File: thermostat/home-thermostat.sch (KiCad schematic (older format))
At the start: 12 parts, among them J1 Thermosthat, U3 LM2574M-5, U4 LD1117S33TR_SOT223, U5 AT24C512

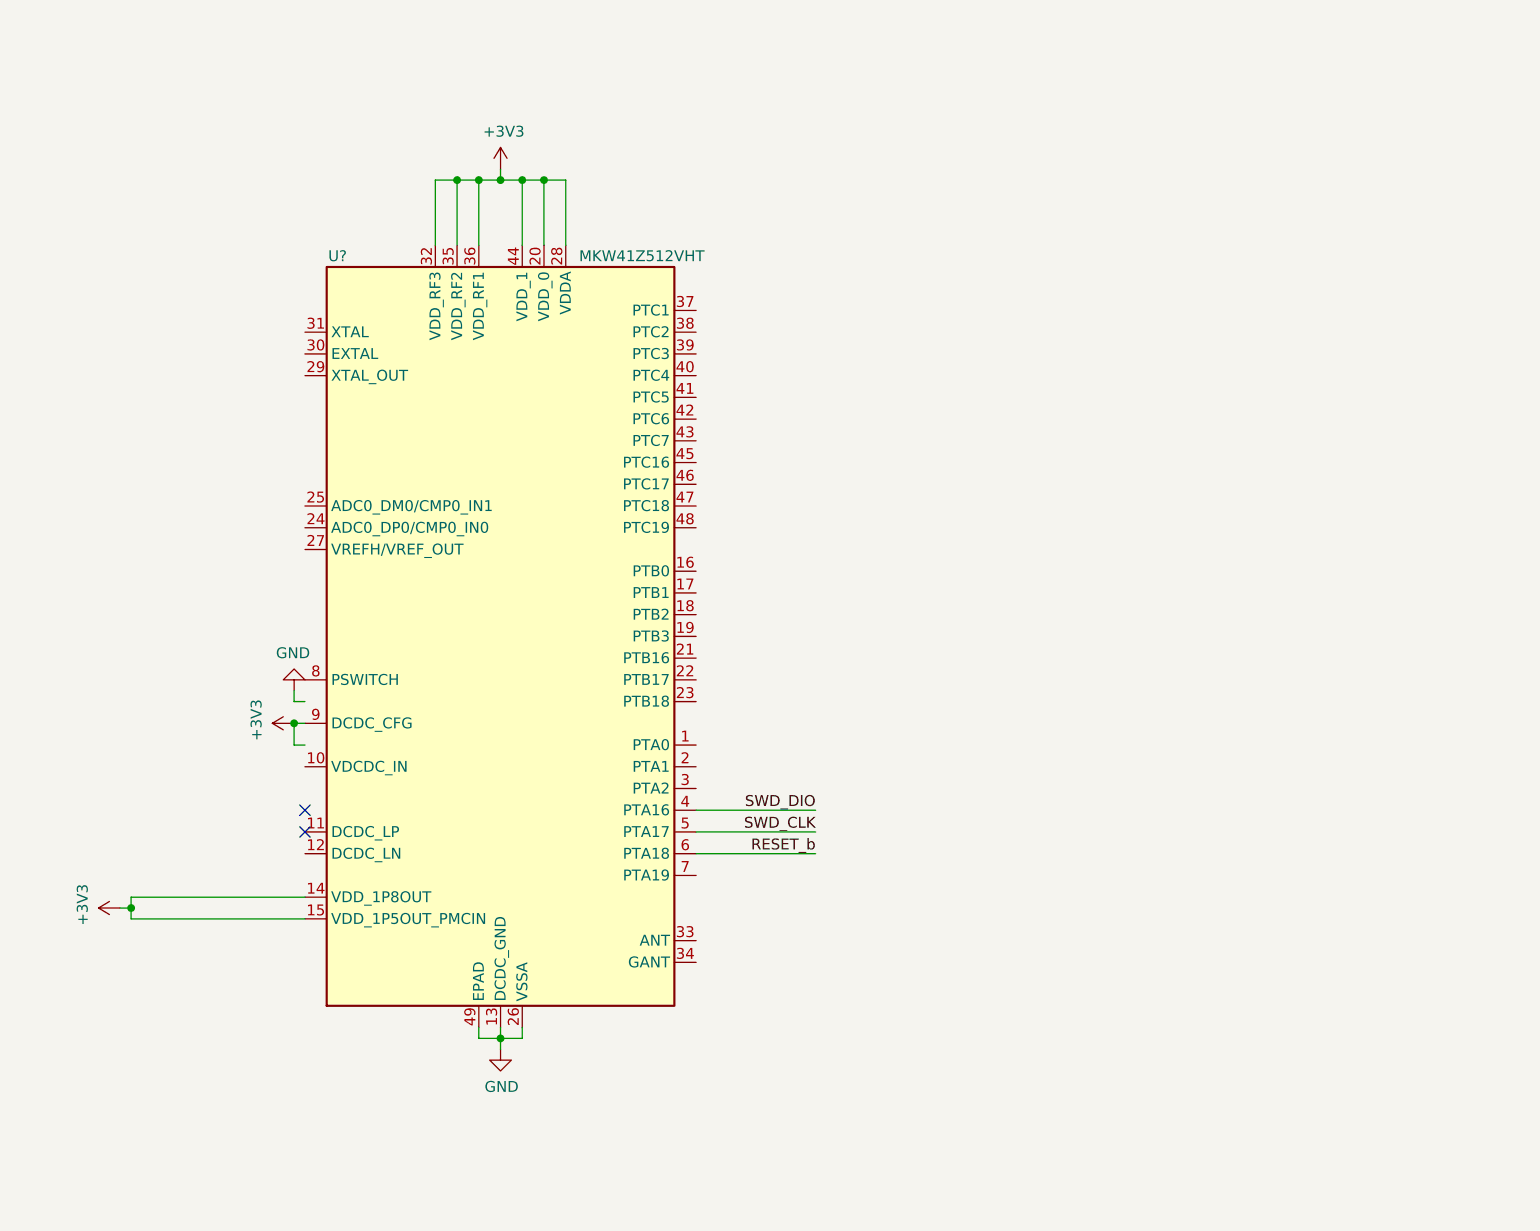
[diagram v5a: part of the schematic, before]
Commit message: Finished minimal connections for MKW41Z (I hope), added design files for FRDM development board to look up antenna connections etc.
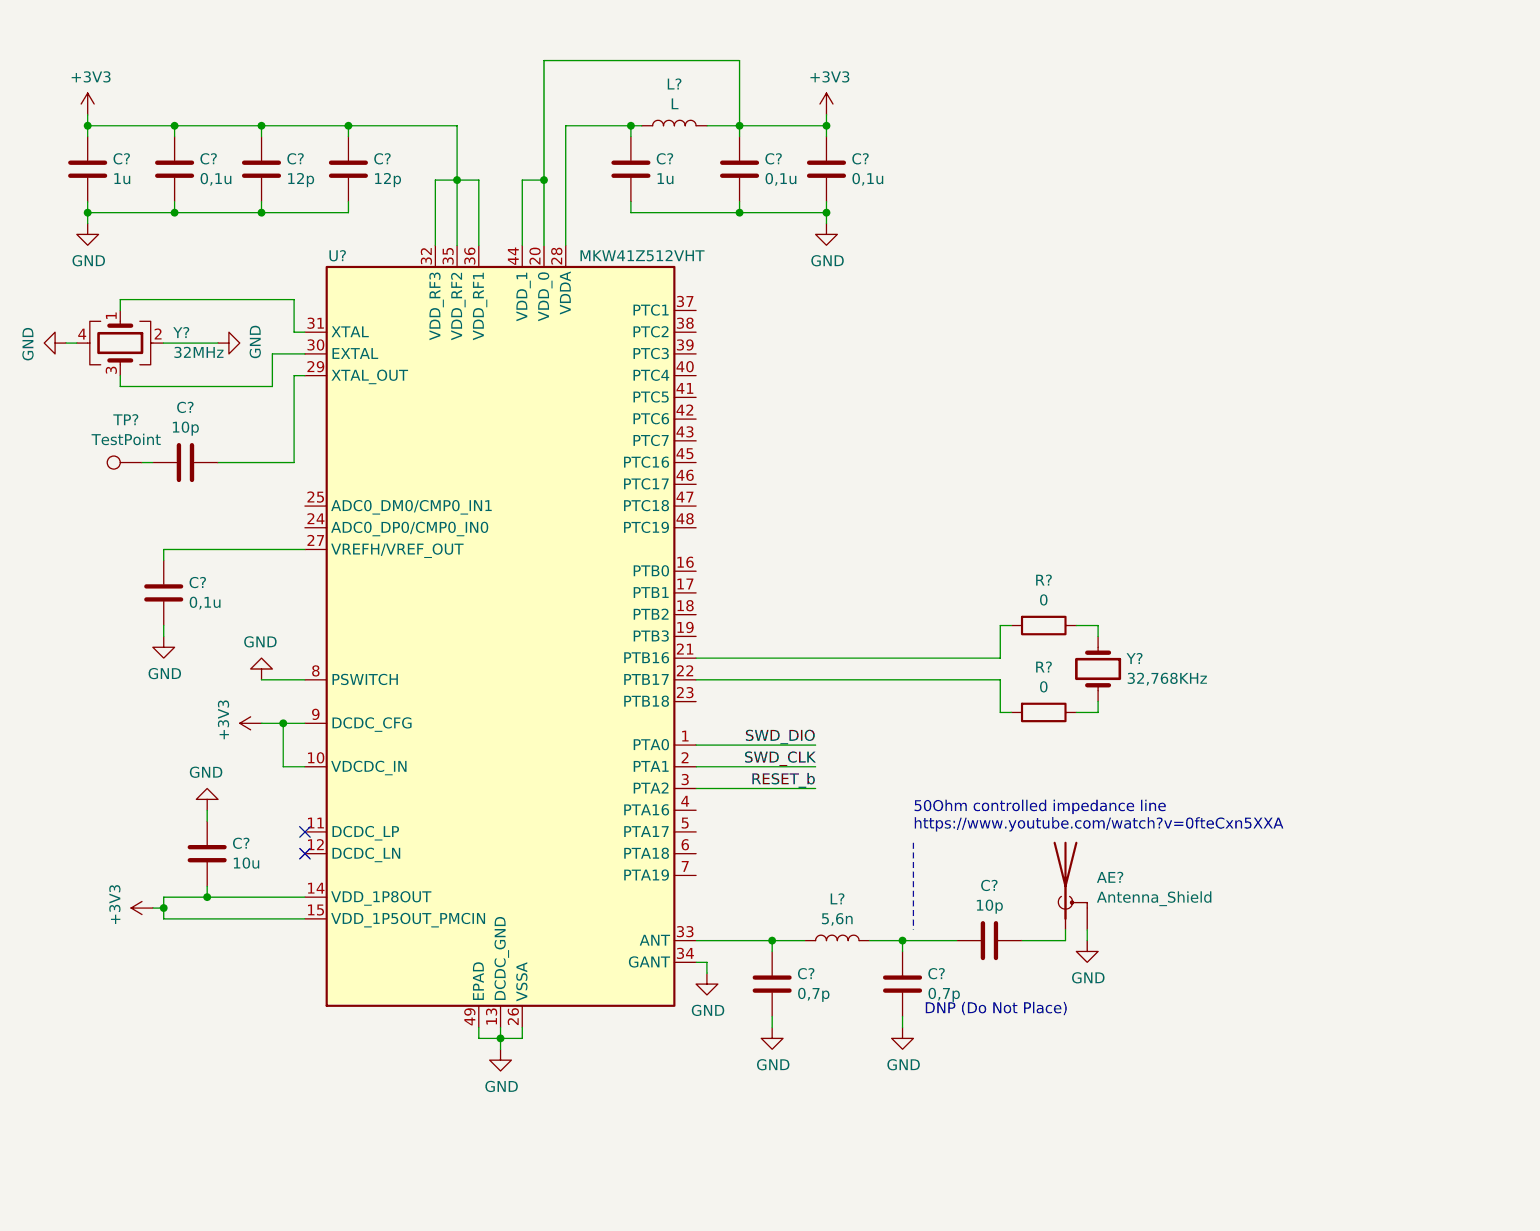
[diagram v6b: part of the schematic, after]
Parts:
- added AE?: Antenna_Shield, symbol Device:Antenna_Shield
- added C? (x2): 1u, symbol Device:C
- added C? (x2): 12p, symbol Device:C
- added C? (x4): 0,1u, symbol Device:C
- added C?: 10u, symbol Device:C
- added C? (x2): 0,7p, symbol Device:C
- added C? (x2): 10p, symbol Device:C
- added L?: L, symbol Device:L
- added L?: 5,6n, symbol Device:L
- added R? (x2): 0, symbol Device:R
- added TP?: TestPoint, symbol Connector:TestPoint
- added Y?: 32MHz, symbol Device:Crystal_GND24
- added Y?: 32,768KHz, symbol Device:Crystal
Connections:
- net +3V3: now also U?.10 (VDCDC_IN), C?.1, C?.1, C?.1, C?.1, C?.1, C?.1, C?.1, L?.2; no longer U?.28 (VDDA)
- net GND: now also U?.34 (GANT), U?.8 (PSWITCH), AE?.2 (Shield), C?.2, C?.2, C?.2, C?.2, C?.2, C?.2, C?.2, C?.2, C?.2, C?.2, C?.2, Y?.2, Y?.4
- net RESET_b: now also U?.3 (PTA2); no longer U?.6 (PTA18)
- net SWD_CLK: now also U?.2 (PTA1); no longer U?.5 (PTA17)
- net SWD_DIO: now also U?.1 (PTA0); no longer U?.4 (PTA16)
- net at U?.21 (PTB16): now also R?.2
- net at U?.22 (PTB17): now also R?.2
- net at U?.27 (VREFH/VREF_OUT): now also C?.1
- net at U?.29 (XTAL_OUT): now also C?.1
- net at U?.30 (EXTAL): now also Y?.3
- net at U?.31 (XTAL): now also Y?.1
- net at U?.33 (ANT): now also C?.1, L?.1
- new net: C?.1, L?.1, U?.28 (VDDA)
- new net: C?.1, C?.2, L?.2
- new net: AE?.1 (A), C?.1
- new net: C?.2, TP?.1
- new net: R?.1, Y?.1
- new net: R?.1, Y?.2
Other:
- note added: "50Ohm controlled impedance line\nhttps://www.youtube.com/watch?v=0fteCxn5XXA"
- note added: "DNP (Do Not Place)"

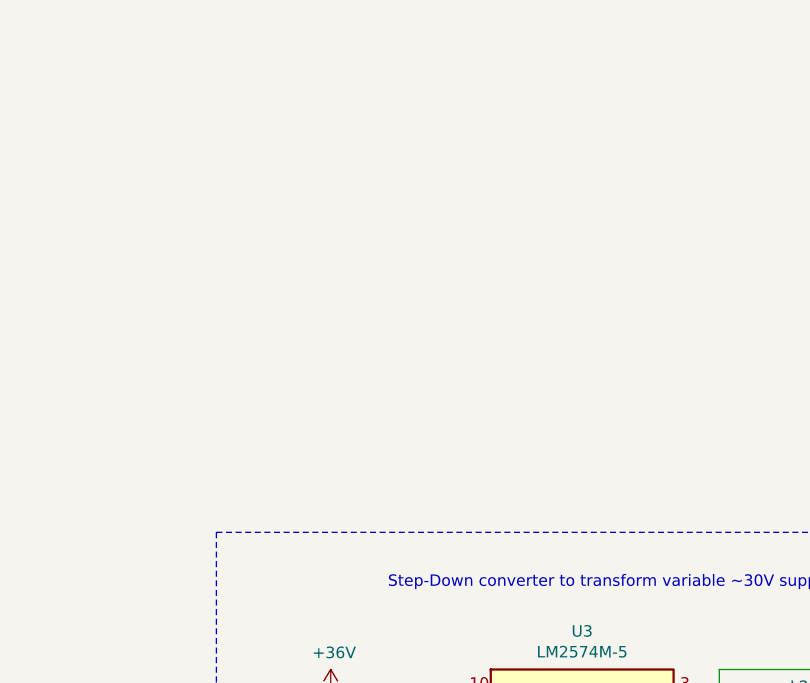
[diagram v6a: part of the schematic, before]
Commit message: Added manual reset button to schematic. Might come handy sometime.
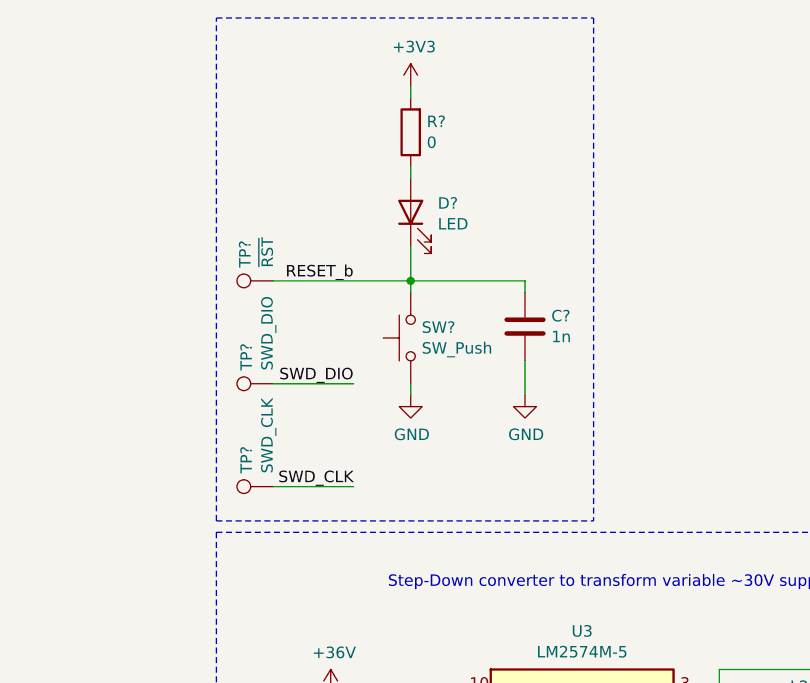
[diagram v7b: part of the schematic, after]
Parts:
- added C?: 1n, symbol Device:C
- added D?: LED, symbol Device:LED
- added R?: 0, symbol Device:R
- added SW?: SW_Push, symbol Switch:SW_Push
- added TP?: ~RST, symbol Connector:TestPoint
- added TP?: SWD_DIO, symbol Connector:TestPoint
- added TP?: SWD_CLK, symbol Connector:TestPoint
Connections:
- net +3V3: now also R?.2
- net GND: now also C?.2, SW?.1
- net RESET_b: now also C?.1, D?.1 (K), SW?.2, TP?.1
- net SWD_CLK: now also TP?.1
- net SWD_DIO: now also TP?.1
- new net: D?.2 (A), R?.1
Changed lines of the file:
@@
 Wire Notes Line
 	7300 4400 7300 4800
+$Comp
+L Connector:TestPoint TP?
+U 1 1 5F494ECC
+P 12900 -500
+F 0 "TP?" H 12958 -376 50  0000 L CNN
+F 1 "~RST" H 12958 -474 50  0000 L CNN
+F 2 "" H 13100 -500 50  0001 C CNN
+F 3 "~" H 13100 -500 50  0001 C CNN
+	1    12900 -500
+	0    -1   -1   0
+$EndComp
+$Comp
+L Connector:TestPoint TP?
+U 1 1 5F4957B3
+P 12900 -50
+F 0 "TP?" H 12958 68  50  0000 L CNN
+F 1 "SWD_DIO" H 12958 -23 50  0000 L CNN
+F 2 "" H 13100 -50 50  0001 C CNN
+F 3 "~" H 13100 -50 50  0001 C CNN
+	1    12900 -50
+	0    -1   -1   0
+$EndComp
+$Comp
+L Connector:TestPoint TP?
+U 1 1 5F495C1A
+P 12900 400
+F 0 "TP?" H 12958 518 50  0000 L CNN
+F 1 "SWD_CLK" H 12958 427 50  0000 L CNN
+F 2 "" H 13100 400 50  0001 C CNN
+F 3 "~" H 13100 400 50  0001 C CNN
+	1    12900 400
+	0    -1   -1   0
+$EndComp
+$Comp
+L power:+3V3 #PWR?
+U 1 1 5F49EC2C
+P 13500 -1350
+AR Path="/5E8AC4D3/5F49EC2C" Ref="#PWR?"  Part="1"
+AR Path="/5F49EC2C" Ref="#PWR?"  Part="1"
+F 0 "#PWR?" H 13500 -1500 50  0001 C CNN
+F 1 "+3V3" H 13515 -1177 50  0000 C CNN
+F 2 "" H 13500 -1350 50  0001 C CNN
+F 3 "" H 13500 -1350 50  0001 C CNN
+	1    13500 -1350
+	1    0    0    -1
+$EndComp
+$Comp
+L Device:LED D?
+U 1 1 5F4A1DA7
+P 13500 -800
+F 0 "D?" V 13539 -918 50  0000 R CNN
+F 1 "LED" V 13448 -918 50  0000 R CNN
+F 2 "" H 13500 -800 50  0001 C CNN
+F 3 "~" H 13500 -800 50  0001 C CNN
+	1    13500 -800
+	0    -1   -1   0
+$EndComp
+$Comp
+L Device:C C?
+U 1 1 5F4A3B33
+P 14000 -300
+F 0 "C?" H 14115 -254 50  0000 L CNN
+F 1 "1n" H 14115 -345 50  0000 L CNN
+F 2 "" H 14038 -450 50  0001 C CNN
+F 3 "~" H 14000 -300 50  0001 C CNN
+	1    14000 -300
+	1    0    0    -1
+$EndComp
+$Comp
+L Switch:SW_Push SW?
+U 1 1 5F4A5C6E
+P 13500 -250
+F 0 "SW?" V 13546 -298 50  0000 R CNN
+F 1 "SW_Push" V 13455 -298 50  0000 R CNN
+F 2 "" H 13500 -50 50  0001 C CNN
+F 3 "~" H 13500 -50 50  0001 C CNN
+	1    13500 -250
+	0    -1   -1   0
+$EndComp
+$Comp
+L power:GND #PWR?
+U 1 1 5F4A6AAA
+P 13500 0
+AR Path="/5E8AC4D3/5F4A6AAA" Ref="#PWR?"  Part="1"
+AR Path="/5F4A6AAA" Ref="#PWR?"  Part="1"
+F 0 "#PWR?" H 13500 -250 50  0001 C CNN
+F 1 "GND" H 13505 -173 50  0000 C CNN
+F 2 "" H 13500 0   50  0001 C CNN
+F 3 "" H 13500 0   50  0001 C CNN
+	1    13500 0
+	1    0    0    -1
+$EndComp
+$Comp
+L power:GND #PWR?
+U 1 1 5F4A6F95
+P 14000 0
+AR Path="/5E8AC4D3/5F4A6F95" Ref="#PWR?"  Part="1"
+AR Path="/5F4A6F95" Ref="#PWR?"  Part="1"
+F 0 "#PWR?" H 14000 -250 50  0001 C CNN
+F 1 "GND" H 14005 -173 50  0000 C CNN
+F 2 "" H 14000 0   50  0001 C CNN
+F 3 "" H 14000 0   50  0001 C CNN
+	1    14000 0
+	1    0    0    -1
+$EndComp
+Wire Wire Line
+	13500 -1000 13500 -950
+Wire Wire Line
+	13500 -650 13500 -500
+Wire Wire Line
+	14000 -450 14000 -500
+Wire Wire Line
+	14000 -500 13500 -500
+Connection ~ 13500 -500
+Wire Wire Line
+	13500 -500 13500 -450
+Wire Wire Line
+	13500 -50  13500 0
+Wire Wire Line
+	14000 -150 14000 0
+Text Label 13250 -50  2    50   ~ 0
+SWD_DIO
+Text Label 13250 400  2    50   ~ 0
+SWD_CLK
+Text Label 13250 -500 2    50   ~ 0
+RESET_b
+Wire Wire Line
+	12900 -500 13500 -500
+Wire Wire Line
+	13250 -50  12900 -50
+Wire Wire Line
+	13250 400  12900 400
+$Comp
+L Device:R R?
+U 1 1 5F504E9C
+P 13500 -1150
+F 0 "R?" H 13430 -1196 50  0000 R CNN
+F 1 "0" H 13430 -1105 50  0000 R CNN
+F 2 "" V 13430 -1150 50  0001 C CNN
+F 3 "~" H 13500 -1150 50  0001 C CNN
+	1    13500 -1150
+	-1   0    0    1
+$EndComp
+Wire Wire Line
+	13500 -1350 13500 -1300
+Wire Notes Line
+	12650 550  12650 -1650
+Wire Notes Line
+	12650 -1650 14300 -1650
+Wire Notes Line
+	14300 -1650 14300 550
+Wire Notes Line
+	12650 550  14300 550
 $EndSCHEMATC

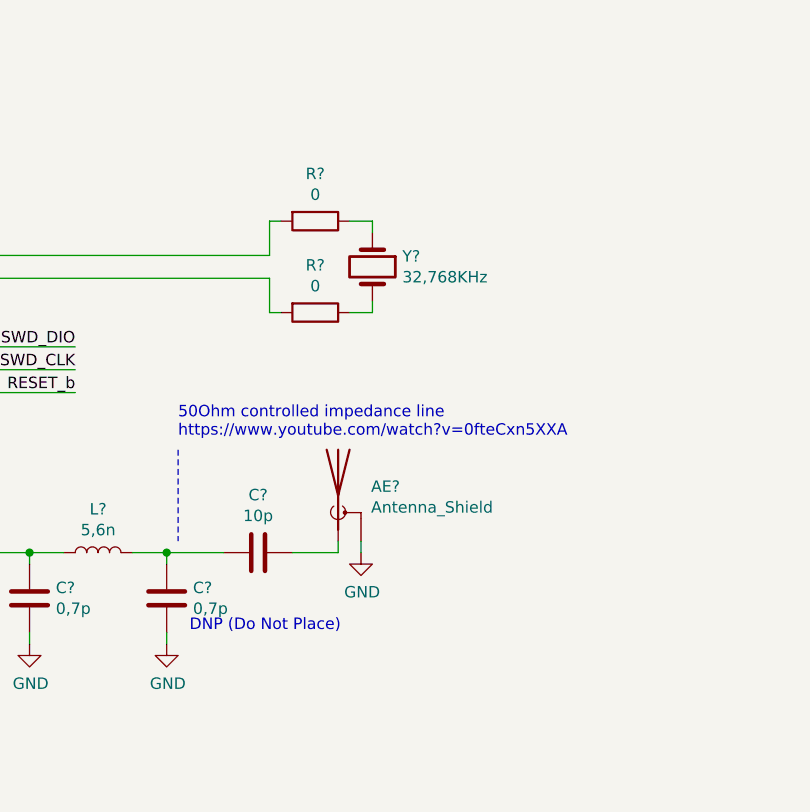
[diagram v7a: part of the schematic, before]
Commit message: Removed 0Ohm capacitor from 32,768KHz crystal as it was only for bypassing crystal in evalboard if the MCU pin is used otherwise.
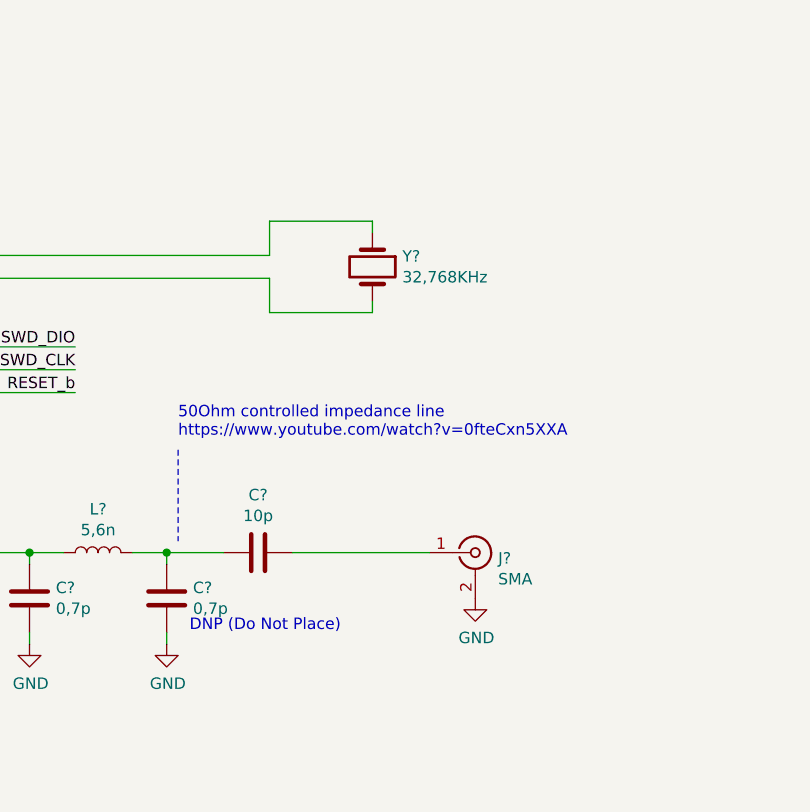
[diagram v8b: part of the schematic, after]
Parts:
- removed AE?: Antenna_Shield, symbol Device:Antenna_Shield
- removed R? (x2): 0, symbol Device:R
- added J?: SMA, symbol Connector:Conn_Coaxial
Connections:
- net GND: now also J?.2 (Ext)
- net at U?.21 (PTB16): now also Y?.1
- net at U?.22 (PTB17): now also Y?.2
- net at C?.1: now also J?.1 (In)
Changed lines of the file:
@@
-$EndComp
-$Comp
-L Device:Antenna_Shield AE?
-U 1 1 5F3CD4FE
-P 8000 4600
-F 0 "AE?" H 8144 4639 50  0000 L CNN
-F 1 "Antenna_Shield" H 8144 4548 50  0000 L CNN
-F 2 "" H 8000 4700 50  0001 C CNN
-F 3 "~" H 8000 4700 50  0001 C CNN
-	1    8000 4600
-	1    0    0    -1
 $EndComp
 $Comp
 L power:GND #PWR?
 U 1 1 5F3CDD8C
-P 8100 4850
+P 8600 5050
 AR Path="/5E8AC4D3/5F3CDD8C" Ref="#PWR?"  Part="1"
 AR Path="/5F3CDD8C" Ref="#PWR?"  Part="1"
-F 0 "#PWR?" H 8100 4600 50  0001 C CNN
-F 1 "GND" H 8105 4677 50  0000 C CNN
-F 2 "" H 8100 4850 50  0001 C CNN
-F 3 "" H 8100 4850 50  0001 C CNN
-	1    8100 4850
-	1    0    0    -1
-$EndComp
-Wire Wire Line
-	8100 4800 8100 4850
-Wire Wire Line
-	7800 4850 8000 4850
-Wire Wire Line
-	8000 4850 8000 4800
+F 0 "#PWR?" H 8600 4800 50  0001 C CNN
+F 1 "GND" H 8605 4877 50  0000 C CNN
+F 2 "" H 8600 5050 50  0001 C CNN
+F 3 "" H 8600 5050 50  0001 C CNN
+	1    8600 5050
+	1    0    0    -1
+$EndComp
 Wire Wire Line
 	7500 4850 7250 4850
@@
 	0    1    1    0
 $EndComp
-$Comp
-L Device:R R?
-U 1 1 5F446CC8
-P 7900 3400
-F 0 "R?" V 7693 3400 50  0000 C CNN
-F 1 "0" V 7784 3400 50  0000 C CNN
-F 2 "" V 7830 3400 50  0001 C CNN
-F 3 "~" H 7900 3400 50  0001 C CNN
-	1    7900 3400
-	0    1    1    0
-$EndComp
-$Comp
-L Device:R R?
-U 1 1 5F447413
-P 7900 3800
-F 0 "R?" V 7693 3800 50  0000 C CNN
-F 1 "0" V 7784 3800 50  0000 C CNN
-F 2 "" V 7830 3800 50  0001 C CNN
-F 3 "~" H 7900 3800 50  0001 C CNN
-	1    7900 3800
-	0    1    1    0
-$EndComp
 Wire Wire Line
 	6300 3550 7700 3550
@@
 	6300 3650 7700 3650
 Wire Wire Line
-	7700 3400 7750 3400
-Wire Wire Line
 	7700 3400 7700 3550
 Wire Wire Line
 	7700 3650 7700 3800
 Wire Wire Line
-	7700 3800 7750 3800
-Wire Wire Line
-	8050 3800 8150 3800
-Wire Wire Line
 	8150 3800 8150 3750
 Wire Wire Line
 	8150 3450 8150 3400
-Wire Wire Line
-	8150 3400 8050 3400
 Text Notes 7300 4350 0    50   ~ 0
 50Ohm controlled impedance line\nhttps://www.youtube.com/watch?v=0fteCxn5XXA
@@
 Wire Notes Line
 	12650 550  14300 550
+$Comp
+L Connector:Conn_Coaxial J?
+U 1 1 5F529E82
+P 8600 4850
+F 0 "J?" H 8700 4825 50  0000 L CNN
+F 1 "SMA" H 8700 4734 50  0000 L CNN
+F 2 "" H 8600 4850 50  0001 C CNN
+F 3 " ~" H 8600 4850 50  0001 C CNN
+	1    8600 4850
+	1    0    0    -1
+$EndComp
+Wire Wire Line
+	7800 4850 8400 4850
+Wire Wire Line
+	7700 3400 8150 3400
+Wire Wire Line
+	7700 3800 8150 3800
 $EndSCHEMATC
